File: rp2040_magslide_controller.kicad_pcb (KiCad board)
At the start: 4 copper layers, 16 x 53.4 mm, 39 parts, among them J1 Pressure sensor, J2 50-00174, J3 Conn_02x05_Odd_Even, U1 W25Q64JV, U2 AP2112K-3.3, U3 RP2040, U4 LIS3DH, U5 SGM3157, Y1 12Mhz

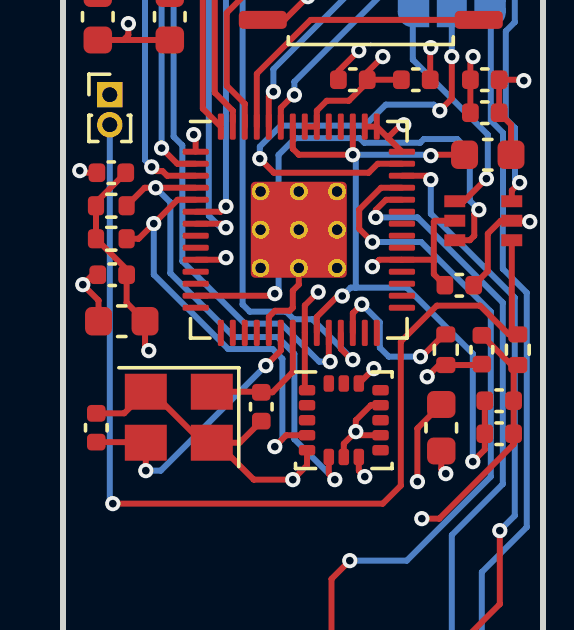
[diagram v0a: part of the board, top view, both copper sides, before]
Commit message: Updated JLCPCB
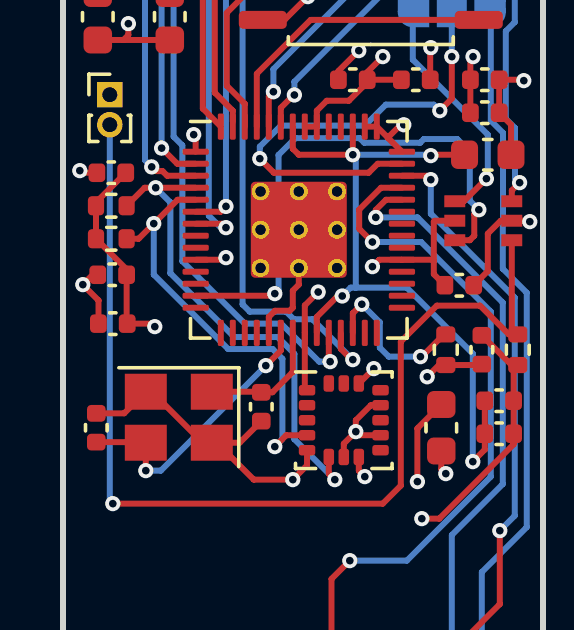
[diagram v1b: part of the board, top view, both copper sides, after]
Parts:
- C18: footprint Capacitor_SMD:C_0603_1608Metric -> Capacitor_SMD:C_0402_1005Metric
- moved C18 0.31 mm to (172.3, 101.6)
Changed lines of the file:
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@@
+    )
+  )
+  (footprint "Capacitor_SMD:C_0402_1005Metric" (layer "F.Cu")
+    (at 172.3 101.6 180)
+    (descr "Capacitor SMD 0402 (1005 Metric), square (rectangular) end terminal, IPC_7351 nominal, (Body size source: IPC-SM-782 page 76, https://www.pcb-3d.com/wordpress/wp-content/uploads/ipc-sm-782a_amendment_1_and_2.pdf), generated with kicad-footprint-generator")
+    (tags "capacitor")
+    (property "Sheetfile" "rp2040_magslide_controller.kicad_sch")
+    (property "Sheetname" "")
+    (attr smd)
+    (fp_text reference "C18" (at 0 -1.16) (layer "Dwgs.User")
+      (effects (font (size 1 1) (thickness 0.15)))
+    )
+    (fp_text value "100nF" (at 0 1.16) (layer "F.Fab")
+      (effects (font (size 1 1) (thickness 0.15)))
+    )
+    (fp_text user "${REFERENCE}" (at 0 0) (layer "F.Fab")
+      (effects (font (size 0.25 0.25) (thickness 0.04)))
+    )
+    (fp_line (start -0.107836 0.36) (end 0.107836 0.36) (layer "F.SilkS") (width 0.12))
+    (fp_line (start -0.107836 -0.36) (end 0.107836 -0.36) (layer "F.SilkS") (width 0.12))
+    (fp_line (start -0.91 -0.46) (end 0.91 -0.46) (layer "F.CrtYd") (width 0.05))
+    (fp_line (start 0.91 0.46) (end -0.91 0.46) (layer "F.CrtYd") (width 0.05))
+    (fp_line (start -0.91 0.46) (end -0.91 -0.46) (layer "F.CrtYd") (width 0.05))
+    (fp_line (start 0.91 -0.46) (end 0.91 0.46) (layer "F.CrtYd") (width 0.05))
+    (fp_line (start 0.5 -0.25) (end 0.5 0.25) (layer "F.Fab") (width 0.1))
+    (fp_line (start -0.5 -0.25) (end 0.5 -0.25) (layer "F.Fab") (width 0.1))
+    (fp_line (start -0.5 0.25) (end -0.5 -0.25) (layer "F.Fab") (width 0.1))
+    (fp_line (start 0.5 0.25) (end -0.5 0.25) (layer "F.Fab") (width 0.1))
+    (pad "1" smd roundrect locked (at -0.48 0 180) (size 0.56 0.62) (layers "F.Cu" "F.Paste" "F.Mask") (roundrect_rratio 0.25)
+      (net 1 "+3V3") (pintype "passive"))
+    (pad "2" smd roundrect locked (at 0.48 0 180) (size 0.56 0.62) (layers "F.Cu" "F.Paste" "F.Mask") (roundrect_rratio 0.25)
+      (net 2 "GND") (pintype "passive"))
+    (model "${KICAD6_3DMODEL_DIR}/Capacitor_SMD.3dshapes/C_0402_1005Metric.wrl"
+      (offset (xyz 0 0 0))
+      (scale (xyz 1 1 1))
+      (rotate (xyz 0 0 0))
     )
   )
@@
     (property "Sheetfile" "rp2040_magslide_controller.kicad_sch")
     (property "Sheetname" "")
-    (attr through_hole)
+    (attr through_hole exclude_from_pos_files exclude_from_bom)
     (fp_text reference "J1" (at 0 -1.56) (layer "Dwgs.User")
       (effects (font (size 1 1) (thickness 0.15)))
@@
     )
   )
-  (footprint "Capacitor_SMD:C_0603_1608Metric" (layer "F.Cu")
-    (at 172.6 101.52 180)
-    (descr "Capacitor SMD 0603 (1608 Metric), square (rectangular) end terminal, IPC_7351 nominal, (Body size source: IPC-SM-782 page 76, https://www.pcb-3d.com/wordpress/wp-content/uploads/ipc-sm-782a_amendment_1_and_2.pdf), generated with kicad-footprint-generator")
-    (tags "capacitor")
-    (property "Sheetfile" "rp2040_magslide_controller.kicad_sch")
-    (property "Sheetname" "")
-    (attr smd)
-    (fp_text reference "C18" (at 0 -1.43) (layer "Dwgs.User")
-      (effects (font (size 1 1) (thickness 0.15)))
-    )
-    (fp_text value "100nF" (at 0 1.43) (layer "F.Fab")
-      (effects (font (size 1 1) (thickness 0.15)))
-    )
-    (fp_text user "${REFERENCE}" (at 0 0) (layer "F.Fab")
-      (effects (font (size 0.4 0.4) (thickness 0.06)))
-    )
-    (fp_line (start -0.14058 0.51) (end 0.14058 0.51) (layer "F.SilkS") (width 0.12))
-    (fp_line (start -0.14058 -0.51) (end 0.14058 -0.51) (layer "F.SilkS") (width 0.12))
-    (fp_line (start -1.48 -0.73) (end 1.48 -0.73) (layer "F.CrtYd") (width 0.05))
-    (fp_line (start -1.48 0.73) (end -1.48 -0.73) (layer "F.CrtYd") (width 0.05))
-    (fp_line (start 1.48 0.73) (end -1.48 0.73) (layer "F.CrtYd") (width 0.05))
-    (fp_line (start 1.48 -0.73) (end 1.48 0.73) (layer "F.CrtYd") (width 0.05))
-    (fp_line (start -0.8 -0.4) (end 0.8 -0.4) (layer "F.Fab") (width 0.1))
-    (fp_line (start 0.8 -0.4) (end 0.8 0.4) (layer "F.Fab") (width 0.1))
-    (fp_line (start -0.8 0.4) (end -0.8 -0.4) (layer "F.Fab") (width 0.1))
-    (fp_line (start 0.8 0.4) (end -0.8 0.4) (layer "F.Fab") (width 0.1))
-    (pad "1" smd roundrect locked (at -0.775 0 180) (size 0.9 0.95) (layers "F.Cu" "F.Paste" "F.Mask") (roundrect_rratio 0.25)
-      (net 1 "+3V3") (pintype "passive"))
-    (pad "2" smd roundrect locked (at 0.775 0 180) (size 0.9 0.95) (layers "F.Cu" "F.Paste" "F.Mask") (roundrect_rratio 0.25)
-      (net 2 "GND") (pintype "passive"))
-    (model "${KICAD6_3DMODEL_DIR}/Capacitor_SMD.3dshapes/C_0603_1608Metric.wrl"
-      (offset (xyz 0 0 0))
-      (scale (xyz 1 1 1))
-      (rotate (xyz 0 0 0))
-    )
-  )
   (footprint "Capacitor_SMD:C_0402_1005Metric" (layer "F.Cu")
     (at 185.18 105.27)
@@
     (property "Sheetfile" "rp2040_magslide_controller.kicad_sch")
     (property "Sheetname" "")
-    (attr through_hole)
+    (attr through_hole exclude_from_pos_files exclude_from_bom)
     (fp_text reference "J2" (at 12.5 -8.65 90) (layer "Dwgs.User")
       (effects (font (size 1 1) (thickness 0.15)))
@@
     (property "Sheetfile" "rp2040_magslide_controller.kicad_sch")
     (property "Sheetname" "")
-    (attr exclude_from_pos_files)
+    (attr exclude_from_pos_files exclude_from_bom)
     (fp_text reference "J3" (at 0 2.9 90) (layer "Dwgs.User")
       (effects (font (size 1 1) (thickness 0.15)))
@@
     (property "Sheetfile" "rp2040_magslide_controller.kicad_sch")
     (property "Sheetname" "")
-    (attr exclude_from_pos_files)
+    (attr exclude_from_pos_files exclude_from_bom)
     (fp_text reference "JP1" (at 0 1.8) (layer "Dwgs.User")
       (effects (font (size 1 1) (thickness 0.15)) (justify mirror))
@@
     (property "Sheetfile" "rp2040_magslide_controller.kicad_sch")
     (property "Sheetname" "")
-    (attr exclude_from_pos_files)
+    (attr exclude_from_pos_files exclude_from_bom)
     (fp_text reference "JP2" (at 0 1.8) (layer "Dwgs.User")
       (effects (font (size 1 1) (thickness 0.15)) (justify mirror))
@@
   (segment (start 172.76 99.79) (end 171.74 98.77) (width 0.2) (layer "F.Cu") (net 1))
   (segment (start 180.7 95.0325) (end 181.1 95.0325) (width 0.2) (layer "F.Cu") (net 1))
-  (segment (start 173.375 102.375) (end 173.5 102.5) (width 0.2) (layer "F.Cu") (net 1))
   (segment (start 178.7 103.745) (end 178.7 101.9075) (width 0.2) (layer "F.Cu") (net 1))
   (segment (start 183.03 98.17) (end 183.7 98.17) (width 0.2) (layer "F.Cu") (net 1))
-  (segment (start 173.375 101.52) (end 173.375 102.375) (width 0.2) (layer "F.Cu") (net 1))
   (segment (start 184.22 94.57) (end 184.22 93.47) (width 0.2) (layer "F.Cu") (net 1))
   (segment (start 180.5 106.045) (end 180.5 106.5) (width 0.2) (layer "F.Cu") (net 1))
@@
   (segment (start 179.59 120.8125) (end 180.3875 120.8125) (width 0.2) (layer "F.Cu") (net 1))
   (segment (start 181.4525 117.05) (end 181.4525 116.5475) (width 0.2) (layer "F.Cu") (net 1))
-  (segment (start 172.76 99.97) (end 172.76 100.905) (width 0.2) (layer "F.Cu") (net 1))
+  (segment (start 172.76 101.58) (end 172.78 101.6) (width 0.2) (layer "F.Cu") (net 1))
   (segment (start 183 99.5) (end 183 98.2) (width 0.2) (layer "F.Cu") (net 1))
   (segment (start 180.3875 120.8125) (end 180.6 120.6) (width 0.2) (layer "F.Cu") (net 1))
@@
   (segment (start 183.62 85.38) (end 184 85) (width 0.2) (layer "F.Cu") (net 1))
   (segment (start 181.46875 95.40125) (end 181.1 95.0325) (width 0.2) (layer "F.Cu") (net 1))
+  (segment (start 173.6 101.6) (end 173.7 101.7) (width 0.2) (layer "F.Cu") (net 1))
   (segment (start 175.0625 95.366) (end 175.0625 95.87) (width 0.2) (layer "F.Cu") (net 1))
-  (segment (start 172.76 100.905) (end 173.375 101.52) (width 0.2) (layer "F.Cu") (net 1))
+  (segment (start 172.76 99.97) (end 172.76 101.58) (width 0.2) (layer "F.Cu") (net 1))
   (segment (start 180.78 93.47) (end 180.78 93.22) (width 0.2) (layer "F.Cu") (net 1))
   (segment (start 183.37 100.32) (end 183 99.95) (width 0.2) (layer "F.Cu") (net 1))
@@
   (segment (start 183.25 105.845) (end 183.25 106.45) (width 0.2) (layer "F.Cu") (net 1))
   (segment (start 171.8 90.595) (end 171.8 89.1825) (width 0.2) (layer "F.Cu") (net 1))
+  (segment (start 172.78 101.6) (end 173.6 101.6) (width 0.2) (layer "F.Cu") (net 1))
   (segment (start 176.7125 115.1875) (end 176.7 115.2) (width 0.2) (layer "F.Cu") (net 1))
   (via (at 179.146469 100.546468) (size 0.508) (drill 0.254) (layers "F.Cu" "B.Cu") (net 1))
@@
   (via (at 182 94.97) (size 0.508) (drill 0.254) (layers "F.Cu" "B.Cu") (net 1))
   (via (at 182.779201 103.370537) (size 0.508) (drill 0.254) (layers "F.Cu" "B.Cu") (net 1))
-  (via (at 173.5 102.5) (size 0.508) (drill 0.254) (layers "F.Cu" "B.Cu") (net 1))
   (via (at 171.9 88.1) (size 0.508) (drill 0.254) (layers "F.Cu" "B.Cu") (net 1))
   (via (at 181 103.1) (size 0.508) (drill 0.254) (layers "F.Cu" "B.Cu") (net 1))
@@
   (via (at 181.9 75.5) (size 0.508) (drill 0.254) (layers "F.Cu" "B.Cu") (net 1))
   (via (at 183.4 106.6) (size 0.508) (drill 0.254) (layers "F.Cu" "B.Cu") (net 1))
+  (via (at 173.7 101.7) (size 0.508) (drill 0.254) (layers "F.Cu" "B.Cu") (net 1))
   (via (at 174.9965 95.3) (size 0.508) (drill 0.254) (layers "F.Cu" "B.Cu") (net 1))
   (via (at 175.5 119.9) (size 0.508) (drill 0.254) (layers "F.Cu" "B.Cu") (net 1))
